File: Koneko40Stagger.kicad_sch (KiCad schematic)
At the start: 24 parts, among them J1 Conn_01x04_MountingPin, J4 TC2030_SWD, SW53 SW_Push, U2 3.3V Fixed Regulator, U6 STM32L443CCUx

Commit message: Aug202023-7:30pm
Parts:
- added JP1: Jumper_2_Open, Connector_PinHeader_1.27mm:PinHeader_1x02_P1.27mm_Vertical, symbol Jumper:Jumper_2_Open
- added R1: 10k 0402, Resistor_SMD:R_0402_1005Metric, symbol Device:R_Small_US
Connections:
- net +3.3V: now also JP1.2 (B)
- net COL8: now also U6.11 (PA1); no longer U6.44 (PH3)
- net GND: now also R1.2
- net SWD: now also J4.2 (SWDIO); no longer J4.6 (SWO)
- new net: JP1.1 (A), R1.1, U6.44 (PH3)
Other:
- moved on the sheet: U6

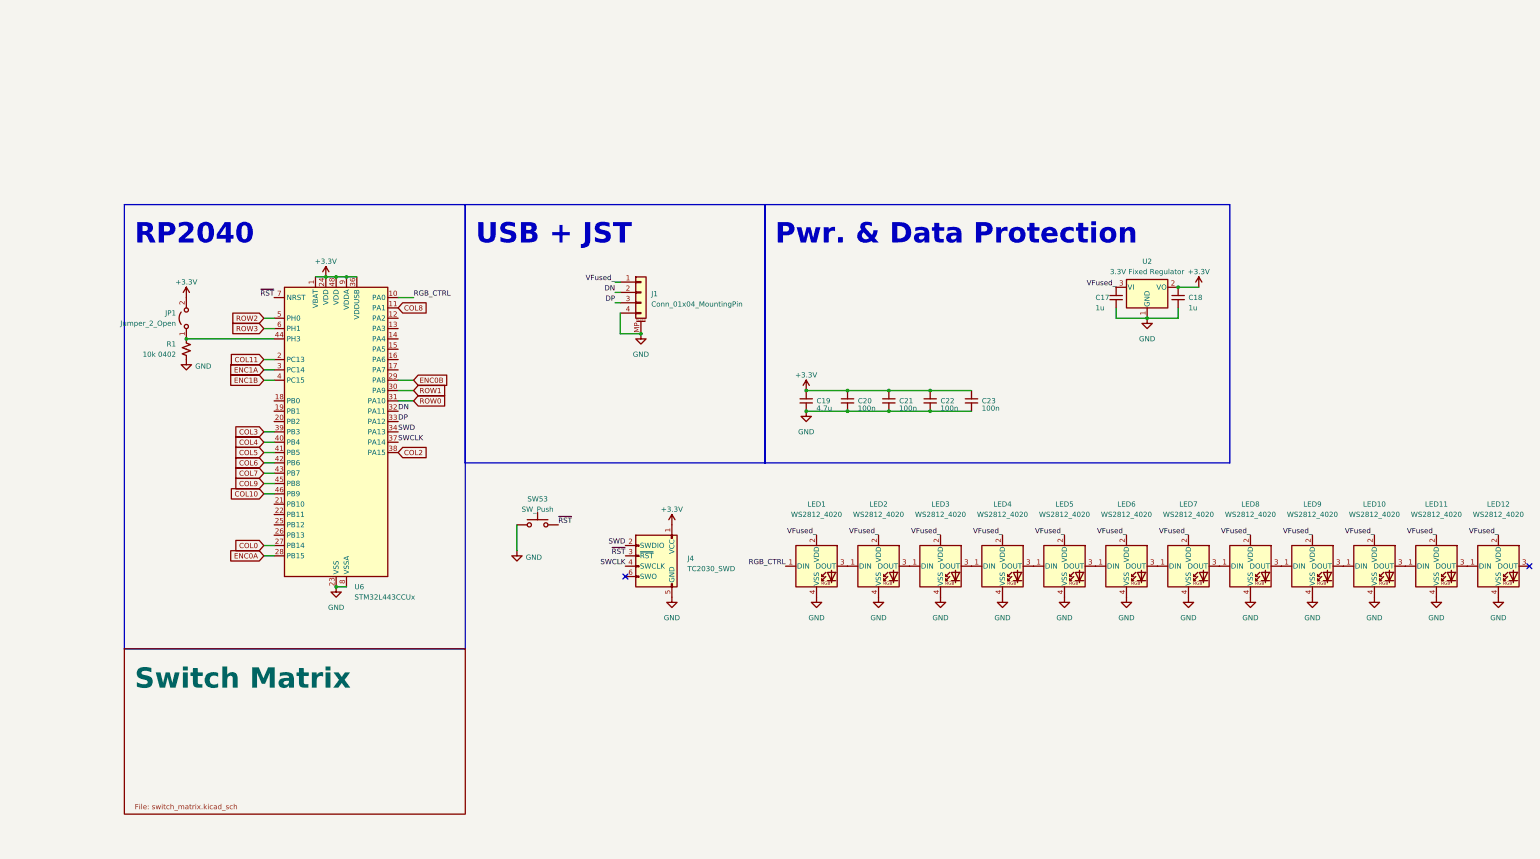
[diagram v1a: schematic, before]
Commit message: Refactored to use RP2040
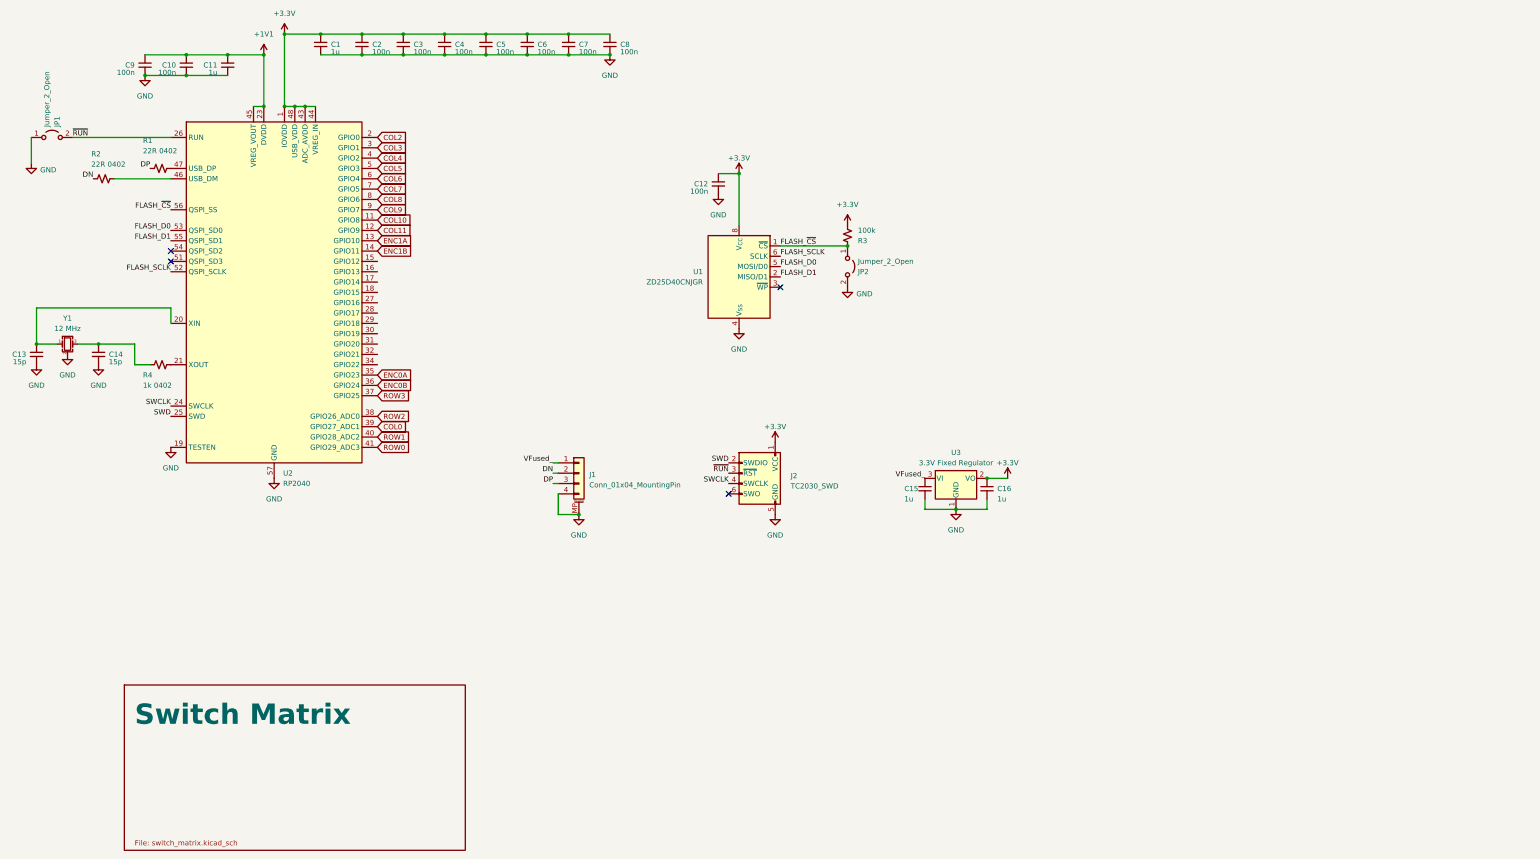
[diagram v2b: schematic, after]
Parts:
- removed C17, C18: 1u, Capacitor_SMD:C_0402_1005Metric, symbol Device:C_Small
- removed C19: 4.7u, Capacitor_SMD:C_0402_1005Metric, symbol Device:C_Small
- removed C20, C21, C22, C23: 100n, Capacitor_SMD:C_0402_1005Metric, symbol Device:C_Small
- removed J4: TC2030_SWD, PCM_marbastlib-various:CON_TC2030_outlined, symbol PCM_marbastlib-various:TC2030_SWD
- removed LED1, LED10, LED11, LED12, LED2, LED3, LED4, LED5, LED6, LED7, LED8, LED9: WS2812_4020, PCM_marbastlib-xp-various:LED_WS2812_4020, symbol marbastlib-various:WS2812_4020
- removed SW53: SW_Push, Button_Switch_SMD:SW_SPST_SKQG_WithoutStem, symbol Switch:SW_Push
- removed U2: 3.3V Fixed Regulator, Package_TO_SOT_SMD:TSOT-23, symbol Regulator_Linear:AP2127N3-1.2
- removed U6: STM32L443CCUx, Package_DFN_QFN:QFN-48-1EP_7x7mm_P0.5mm_EP5.6x5.6mm_ThermalVias, symbol MCU_ST_STM32L4:STM32L443CCUx
- added C1, C11, C15, C16: 1u, Capacitor_SMD:C_0402_1005Metric, symbol Device:C_Small
- added C10, C12, C2, C3, C4, C5, C6, C7, C8, C9: 100n, Capacitor_SMD:C_0402_1005Metric, symbol Device:C_Small
- added C13, C14: 15p, Capacitor_SMD:C_0402_1005Metric, symbol Device:C_Small
- added J2: TC2030_SWD, PCM_marbastlib-various:CON_TC2030_outlined, symbol PCM_marbastlib-various:TC2030_SWD
- added JP2: Jumper_2_Open, Connector_PinHeader_1.27mm:PinHeader_1x02_P1.27mm_Vertical, symbol Jumper:Jumper_2_Open
- added R2: 22R 0402, Resistor_SMD:R_0402_1005Metric, symbol Device:R_Small_US
- added R3: 100k, Resistor_SMD:R_0402_1005Metric, symbol Device:R_Small_US
- added R4: 1k 0402, Resistor_SMD:R_0402_1005Metric, symbol Device:R_Small_US
- added U1: ZD25D40CNJGR, USON8:USON-8_1.5x1.5mm_P0.45mm, symbol Flash_NOR_SPI:ZD25D40CNJGR
- added U2: RP2040, Package_DFN_QFN:QFN-56-1EP_7x7mm_P0.4mm_EP3.2x3.2mm, symbol MCU_RaspberryPi:RP2040
- added U3: 3.3V Fixed Regulator, Package_TO_SOT_SMD:TSOT-23, symbol Regulator_Linear:AP2127N3-1.2
- added Y1: 12 MHz, Crystal:Crystal_SMD_2520-4Pin_2.5x2.0mm, symbol EasyCrystal:Crystal_GND24_Small_EZ
- R1: value 10k 0402 -> 22R 0402; LCSC C60490 -> C25092
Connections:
- net +3.3V: now also C1.1, C12.1, C16.1, C2.1, C3.1, C4.1, C5.1, C6.1, C7.1, C8.1, J2.1 (VCC), R3.2, U1.8 (V_{CC}), U2.1 (IOVDD), U2.10 (IOVDD), U2.22 (IOVDD), U2.33 (IOVDD), U2.42 (IOVDD), U2.43 (ADC_AVDD), U2.44 (VREG_IN), U2.48 (USB_VDD), U2.49 (IOVDD), U3.2 (VO); no longer JP1.2 (B)
- net COL0: now also U2.39 (GPIO27_ADC1)
- net COL10: now also U2.11 (GPIO8)
- net COL11: now also U2.12 (GPIO9)
- net COL2: now also U2.2 (GPIO0)
- net COL3: now also U2.3 (GPIO1)
- net COL4: now also U2.4 (GPIO2)
- net COL5: now also U2.5 (GPIO3)
- net COL6: now also U2.6 (GPIO4)
- net COL7: now also U2.7 (GPIO5)
- net COL8: now also U2.8 (GPIO6)
- net COL9: now also U2.9 (GPIO7)
- net DN: now also R2.2
- net DP: now also R1.2
- net ENC0A: now also U2.35 (GPIO23)
- net ENC0B: now also U2.36 (GPIO24)
- net ENC1A: now also U2.13 (GPIO10)
- net ENC1B: now also U2.14 (GPIO11)
- net GND: now also JP1.1 (A), C1.2, C10.2, C11.2, C12.2, C13.2, C14.2, C15.2, C16.2, C2.2, C3.2, C4.2, C5.2, C6.2, C7.2, C8.2, C9.2, J2.5 (GND), JP2.2 (B), U1.4 (V_{SS}), U1.9 (PAD/V_{SS}), U2.19 (TESTEN), U2.57 (GND), U3.1 (GND), Y1.2, Y1.4; no longer R1.2
- net ROW0: now also U2.41 (GPIO29_ADC3)
- net ROW1: now also U2.40 (GPIO28_ADC2)
- net ROW2: now also U2.38 (GPIO26_ADC0)
- net ROW3: now also U2.37 (GPIO25)
- net SWCLK: now also J2.4 (SWCLK), U2.24 (SWCLK)
- net SWD: now also J2.2 (SWDIO), U2.25 (SWD)
- net VFused_: now also C15.1, U3.3 (VI)
- net at R1.1: now also U2.47 (USB_DP); no longer JP1.1 (A)
- new net: C13.1, U2.20 (XIN), Y1.1
- new net: R4.2, U2.21 (XOUT)
- new net: R2.1, U2.46 (USB_DM)
- new net: C14.1, R4.1, Y1.3
- new net +1V1: C10.1, C11.1, C9.1, U2.23 (DVDD), U2.45 (VREG_VOUT), U2.50 (DVDD)
- new net FLASH_D0: U1.5 (MOSI/D0), U2.53 (QSPI_SD0)
- new net FLASH_D1: U1.2 (MISO/D1), U2.55 (QSPI_SD1)
- new net FLASH_SCLK: U1.6 (SCLK), U2.52 (QSPI_SCLK)
- new net FLASH_~{CS}: JP2.1 (A), R3.1, U1.1 (~{CS}), U2.56 (QSPI_SS)
- new net ~{RUN}: J2.3 (~{RST}), JP1.2 (B), U2.26 (RUN)
- no-connect marks 2 -> 4
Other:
- note removed: "Pwr. & Data Protection"
- note removed: "RP2040"
- note removed: "USB + JST"

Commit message: Fixed resistor part number.
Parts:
- J2: footprint PCM_marbastlib-various:CON_TC2030_outlined -> Connector:Tag-Connect_TC2030-IDC-NL_2x03_P1.27mm_Vertical
- R4: LCSC C60490 -> C11702
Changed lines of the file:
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@@
       (effects (font (size 1.27 1.27)) hide)
     )
-    (property "LCSC" "C60490" (at 21.59 77.47 0)
+    (property "LCSC" "C11702" (at 21.59 77.47 0)
       (effects (font (size 1.27 1.27)) hide)
     )
@@
       (effects (font (size 1.27 1.27)) (justify left))
     )
-    (property "Footprint" "PCM_marbastlib-various:CON_TC2030_outlined" (at 177.8 105.41 90)
-      (effects (font (size 1.27 1.27)) hide)
-    )
+    (property "Footprint" "Connector:Tag-Connect_TC2030-IDC-NL_2x03_P1.27mm_Vertical" (at 177.8 105.41 90)
+      (effects (font (size 1.27 1.27)) hide)
+    )
